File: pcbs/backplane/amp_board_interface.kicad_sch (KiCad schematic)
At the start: 19 parts, among them J4 RJ45_Shielded, J6 RJ45_Shielded, J7 RJ45_Shielded, Q1 MMBT3904, U1 74LVC1G14, U16 74LVC2G02

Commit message: Finished migrating footprint names
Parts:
- TP19: footprint TestPoint:TestPoint_Keystone_5019_Minature -> TestPoint:TestPoint_Keystone_5019_Miniature
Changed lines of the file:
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@@
 			)
 		)
-		(property "Footprint" "TestPoint:TestPoint_Keystone_5019_Minature"
+		(property "Footprint" "TestPoint:TestPoint_Keystone_5019_Miniature"
 			(at 149.86 67.31 0)
 			(effects

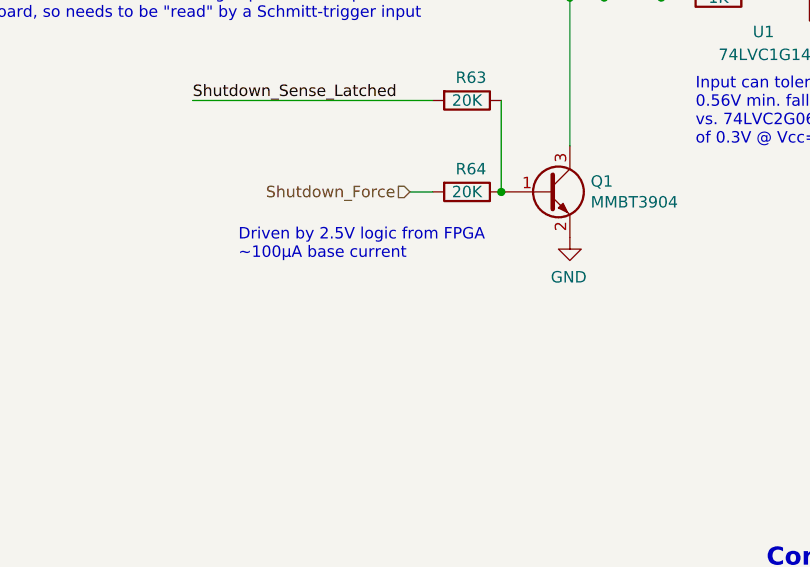
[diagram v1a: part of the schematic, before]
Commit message: BOM & reset fixes
Amp ctrl: changed name of "Manufacturer" field to "MPN" to work with Aisler
Amp ctrl: added part number to logic inverter, corrected various typos and part number problems
Backplane: added pull-down to Shutdown_Reset signal (#35)
Backplane: rethought Shutdown_Force circuit to make fail-safe (broken connections->shutdown), make work correctly (fixes #35)
Backplane: updated/corrected various schematic annotations
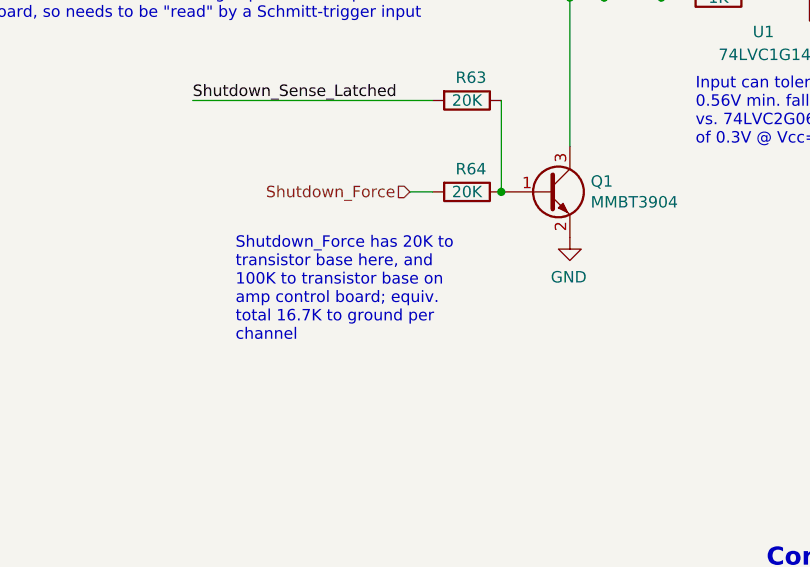
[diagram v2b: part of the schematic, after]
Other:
- note removed: "Driven by 2.5V logic from FPGA ~100µA base current"
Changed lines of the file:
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@@
-		)
-	)
-	(text "Driven by 2.5V logic from FPGA\n~100µA base current"
-		(exclude_from_sim no)
-		(at 60.96 66.04 0)
-		(effects
-			(font
-				(size 1.27 1.27)
-			)
-			(justify left bottom)
 		)
 	)
@@
 		)
 		(effects
+			(font
+				(size 1.27 1.27)
+			)
+			(justify left top)
+		)
+	)
+	(text_box "Shutdown_Force has 20K to transistor base here, and 100K to transistor base on amp control board; equiv. total 16.7K to ground per channel"
+		(exclude_from_sim no)
+		(at 59.69 62.23 0)
+		(size 30.48 13.97)
+		(margins 0.9525 0.9525 0.9525 0.9525)
+		(stroke
+			(width -0.0001)
+			(type solid)
+		)
+		(fill
+			(type none)
+		)
+		(effects
